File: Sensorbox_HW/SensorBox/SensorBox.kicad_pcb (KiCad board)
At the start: 2 copper layers, 77 parts, among them U1 BME280, U11 PS1-O3-100, U12 DS3231M, U13 OPA197xD, U2 OPA197xD, U4 MC33063AD, U5 OPA197xD, U6 MAX31855EASA, U8 HPP845E131R5

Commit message: Sensorbox
Layout erstellt
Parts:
- moved JP1 228.2 mm to (137.0, 49.5), turned to 180 degrees
- moved U7 225.0 mm to (87.5, 61.2), turned to 180 degrees
- moved C2 218.2 mm to (119.9, 98.4), turned to 90 degrees
- moved C1 217.6 mm to (118.0, 98.3), turned to 90 degrees
- moved D4 215.9 mm to (110.5, 54.0), turned to 90 degrees
- moved U1 214.7 mm to (124.0, 97.5), turned to 180 degrees
- moved ADC1 212.6 mm to (135.5, 36.1), turned to -90 degrees
- moved VCC1 212.3 mm to (135.5, 25.9), turned to -90 degrees
- moved GND1 212.2 mm to (135.5, 33.5), turned to -90 degrees
- moved SDA/Signal1 212.0 mm to (135.5, 28.5), turned to -90 degrees
- moved SCL1 212.0 mm to (135.5, 31.0), turned to -90 degrees
- moved U11 211.9 mm to (128.2, 65.0), turned to -90 degrees
- moved D2 210.3 mm to (103.5, 54.1), turned to 90 degrees
- moved C11 207.9 mm to (125.2, 77.5), turned to -90 degrees
- moved U6 207.9 mm to (125.0, 48.5), turned to 180 degrees
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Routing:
- net VDD_3V3: track 0.00 -> 307.6 mm, vias 0 -> 6
- net VDD_5V: track 0.00 -> 261.3 mm, vias 0 -> 3
- net SDA_GPIO21: track 0.00 -> 232.7 mm, vias 0 -> 5
- net SCL_GPIO22: track 0.00 -> 221.9 mm, vias 0 -> 3
- net Mosi_GPIO23: track 0.00 -> 95.9 mm, vias 0 -> 1
- net Miso_GPIO19: track 0.00 -> 89.5 mm, vias 0 -> 2
- net CS_GPIO15: track 0.00 -> 82.4 mm, vias 0 -> 1
- net SCK_GPIO18: track 0.00 -> 80.4 mm, vias 0 -> 2
- net CS_GPIO5: track 0.00 -> 71.1 mm
- net RTC_INIT_GPIO4: track 0.00 -> 59.2 mm, vias 0 -> 1
- net Miso_GPIO12: track 0.00 -> 53.4 mm, vias 0 -> 1
- net RTC_32Khz_GPIO25: track 0.00 -> 52.9 mm, vias 0 -> 1
- net extern_Sensor_Gpio_33: track 0.00 -> 51.1 mm
- net VCC_Bat: track 0.00 -> 50.9 mm
- net VDD_2.5V: track 0.00 -> 47.2 mm, vias 0 -> 1
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- added copper zone on B.Cu, net GND1
- added copper zone on F.Cu, net GND1
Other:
- board outline added: 128.5 x 97.5 mm

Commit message: Layout fertiggestellt
Layout überarbeitet und fertig gestellt
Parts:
- removed D4: 1.5KExxA, Diode_THT:D_DO-201AE_P15.24mm_Horizontal
- removed R14: 4.7k, Resistor_SMD:R_0402_1005Metric
- added C13: 0.1uF, Capacitor_SMD:C_0402_1005Metric_Pad0.74x0.62mm_HandSolder, F.Cu at (105.7, 64.5)
- added C3: 0.1uF, Capacitor_SMD:C_0402_1005Metric_Pad0.74x0.62mm_HandSolder, F.Cu at (111.4, 64.5)
- added C7: 0.1uF, Capacitor_SMD:C_0402_1005Metric_Pad0.74x0.62mm_HandSolder, F.Cu at (120.4, 63.8)
- added D7: PESD3V3U1UA, Diode_SMD:D_SOD-323, F.Cu at (130.0, 27.2)
- added R3: 100R, Resistor_SMD:R_0402_1005Metric, F.Cu at (130.6, 25.1)
- added R4: 100R, Resistor_SMD:R_0402_1005Metric, F.Cu at (131.8, 33.0)
- added R5: 4.7k, Resistor_SMD:R_0402_1005Metric, F.Cu at (78.0, 68.6)
- CO1: value 45.54µF -> 47µF
- D2: value 1.5KExxA -> PESD3V3U1UA; footprint Diode_THT:D_DO-201AE_P15.24mm_Horizontal -> Diode_SMD:D_SOD-323
- L1: value 52µH -> 51µH; footprint Inductor_SMD:L_0402_1005Metric_Pad0.77x0.64mm_HandSolder -> Inductor_SMD:L_0805_2012Metric_Pad1.05x1.20mm_HandSolder
- Rsc1: value 0R41 -> 0R39
- moved TP7 0.31 mm to (74.7, 68.1)
- moved C8 0.20 mm to (73.2, 77.0)
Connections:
- D2 pad 1: SCL_GPIO22 -> Net-(D2-K)
- SCL1 pad 1: SCL_GPIO22 -> Net-(D2-K)
- SDA/Signal1 pad 1: SDA_GPIO21 -> Net-(D7-K)
- U13 pad 7: VDD_5V -> Net-(U13-V+)
- U2 pad 7: VDD_3V3 -> Net-(U2-V+)
- U5 pad 7: VDD_5V -> Net-(U5-V+)
- U7 pad 26: unconnected-(U7-GND-Pad26) -> GND1
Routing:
- net Net-(D2-K): track 0.00 -> 56.6 mm, vias 0 -> 2
- net Net-(D7-K): track 0.00 -> 10.3 mm, vias 0 -> 1
- net VDD_3V3: track 307.6 -> 316.3 mm
- net VDD_5V: track 261.3 -> 254.3 mm, vias 3 -> 5
- net SDA_GPIO21: track 232.7 -> 226.5 mm, vias 5 -> 6
- net Net-(U2-V+): track 0.00 -> 3.88 mm
- net RTC_INIT_GPIO4: track 59.2 -> 62.8 mm
- net Net-(U13-V+): track 0.00 -> 3.11 mm
- net Net-(U5-V+): track 0.00 -> 2.77 mm
- net VDD_2.5V: track 47.2 -> 44.7 mm
- net SCL_GPIO22: track 221.9 -> 219.7 mm
- net RTC_RST_GPIO16: track 46.6 -> 44.8 mm
- net Net-(U4-Ipk): track 26.4 -> 26.9 mm
- net GND1: track 5.78 -> 5.74 mm, vias 48 -> 52

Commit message: Layout fertigstellen
Löcher, Text auf platine
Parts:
- moved TP5 6.53 mm to (57.1, 52.1), turned to 90 degrees
- moved BT1 2.99 mm to (24.4, 64.1)
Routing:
- net Mosi_GPIO23: track 95.9 -> 97.3 mm
- net Net-(D3-A1): track 28.4 -> 29.7 mm
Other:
- outline, holes or cut-outs redrawn
- board text added: "SensorBox V3"
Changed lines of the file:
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@@
 	(footprint "TestPoint:TestPoint_Loop_D1.80mm_Drill1.0mm_Beaded"
 		(layer "F.Cu")
-		(at 56 58.5)
+		(at 57.15 52.07 90)
 		(descr "wire loop with bead as test point, loop diameter 1.8mm, hole diameter 1.0mm")
 		(tags "test point wire loop bead")
 		(property "Reference" "TP5"
-			(at 0.7 2.5 0)
+			(at 0.7 2.5 90)
 			(layer "F.SilkS")
 			(effects
@@
 		)
 		(property "Value" "TestPoint"
-			(at 0 -2.8 0)
+			(at 0 -2.8 90)
 			(layer "F.Fab")
 			(effects
@@
 		)
 		(property "Footprint" "TestPoint:TestPoint_Loop_D1.80mm_Drill1.0mm_Beaded"
-			(at 0 0 0)
+			(at 0 0 90)
 			(unlocked yes)
 			(layer "F.Fab")
@@
 		)
 		(property "Datasheet" ""
-			(at 0 0 0)
+			(at 0 0 90)
 			(unlocked yes)
 			(layer "F.Fab")
@@
 		)
 		(property "Description" "test point"
-			(at 0 0 0)
+			(at 0 0 90)
 			(unlocked yes)
 			(layer "F.Fab")
@@
 		)
 		(fp_line
-			(start -0.9 -0.2)
-			(end 0.9 -0.2)
+			(start 0.9 -0.2)
+			(end 0.9 0.2)
 			(stroke
 				(width 0.12)
@@
 		)
 		(fp_line
-			(start -0.9 0.2)
-			(end -0.9 -0.2)
+			(start -0.9 -0.2)
+			(end 0.9 -0.2)
 			(stroke
 				(width 0.12)
@@
 		)
 		(fp_line
-			(start 0.9 -0.2)
-			(end 0.9 0.2)
+			(start 0.9 0.2)
+			(end -0.9 0.2)
 			(stroke
 				(width 0.12)
@@
 		)
 		(fp_line
-			(start 0.9 0.2)
-			(end -0.9 0.2)
+			(start -0.9 0.2)
+			(end -0.9 -0.2)
 			(stroke
 				(width 0.12)
@@
 		)
 		(fp_text user "${REFERENCE}"
-			(at 0.7 2.5 0)
+			(at 0.7 2.5 90)
 			(layer "F.Fab")
 			(effects
@@
 		)
 		(pad "1" thru_hole circle
-			(at 0 0)
+			(at 0 0 90)
 			(size 2 2)
 			(drill 1)
@@
 	(footprint "Battery_Basket:BatteryHolder_Keystone_2479_3xAAA"
 		(layer "F.Cu")
-		(at 21.3925 64.0825 90)
+		(at 24.384 64.0825 90)
 		(descr "Keystone Battery Holder, 2479, Battery Type 3xAAA (Script generated with StandardBox.py) (Keystone Battery Holder, 2479, Battery Type 3xAAA)")
 		(tags "Keystone Battery Holder 2479 Battery Type 3xAAA")
@@
 		)
 	)
+	(gr_circle
+		(center 13.716 108.204)
+		(end 13.716 107.188)
+		(stroke
+			(width 0.05)
+			(type default)
+		)
+		(fill none)
+		(layer "Edge.Cuts")
+	)
 	(gr_rect
 		(start 12 12.5)
@@
 		(layer "Edge.Cuts")
 	)
+	(gr_circle
+		(center 138.684 108.204)
+		(end 138.684 107.188)
+		(stroke
+			(width 0.05)
+			(type default)
+		)
+		(fill none)
+		(layer "Edge.Cuts")
+	)
+	(gr_circle
+		(center 13.716 14.224)
+		(end 13.716 13.208)
+		(stroke
+			(width 0.05)
+			(type default)
+		)
+		(fill none)
+		(layer "Edge.Cuts")
+	)
+	(gr_circle
+		(center 138.684 14.224)
+		(end 138.684 13.208)
+		(stroke
+			(width 0.05)
+			(type default)
+		)
+		(fill none)
+		(layer "Edge.Cuts")
+	)
+	(gr_text "SensorBox V3"
+		(at 136.906 107.95 90)
+		(layer "F.SilkS")
+		(effects
+			(font
+				(size 3 3)
+				(thickness 0.3)
+				(bold yes)
+			)
+			(justify left bottom)
+		)
+	)
 	(segment
 		(start 127.203 43.4)
@@
 	)
 	(segment
+		(start 21.3925 80.518)
+		(end 21.3925 80.9108)
+		(width 0.2)
+		(layer "B.Cu")
+		(net 2)
+	)
+	(segment
+		(start 21.3925 80.518)
+		(end 21.3925 68.5235)
+		(width 0.2)
+		(layer "B.Cu")
+		(net 2)
+	)
+	(segment
+		(start 23.368 66.548)
+		(end 23.368 65.0985)
+		(width 0.2)
+		(layer "B.Cu")
+		(net 2)
+	)
+	(segment
 		(start 16.5 80.46)
 		(end 21.3925 80.46)
@@
 	(segment
 		(start 21.3925 80.46)
-		(end 21.3925 80.9108)
+		(end 21.3925 80.518)
 		(width 0.2)
 		(layer "B.Cu")
@@
 	)
 	(segment
-		(start 25 84.5183)
-		(end 25 86.12)
+		(start 23.368 65.0985)
+		(end 24.384 64.0825)
 		(width 0.2)
 		(layer "B.Cu")
@@
 	)
 	(segment
-		(start 21.3925 64.0825)
-		(end 21.3925 80.46)
+		(start 21.3925 68.5235)
+		(end 23.368 66.548)
+		(width 0.2)
+		(layer "B.Cu")
+		(net 2)
+	)
+	(segment
+		(start 25 84.5183)
+		(end 25 86.12)
 		(width 0.2)
 		(layer "B.Cu")
@@
 	)
 	(via
-		(at 15.5 106)
+		(at 18.034 100.838)
 		(size 0.6)
 		(drill 0.3)
@@
 	)
 	(via
-		(at 137.5 15)
+		(at 129.794 13.716)
 		(size 0.6)
 		(drill 0.3)
@@
 	)
 	(segment
+		(start 58.928 52.07)
+		(end 57.15 52.07)
+		(width 0.2)
+		(layer "F.Cu")
+		(net 17)
+	)
+	(segment
 		(start 111.702 18.2392)
 		(end 112.345 18.2392)
@@
 	)
 	(segment
-		(start 60.843 58.5)
-		(end 60.843 55.6857)
+		(start 60.843 55.6857)
+		(end 59.944 54.7867)
 		(width 0.2)
 		(layer "F.Cu")
@@
 	)
 	(segment
-		(start 56 58.5)
-		(end 60.843 58.5)
+		(start 60.843 58.5)
+		(end 60.843 55.6857)
 		(width 0.2)
 		(layer "F.Cu")
@@
 	)
 	(segment
+		(start 59.944 54.7867)
+		(end 59.944 53.086)
+		(width 0.2)
+		(layer "F.Cu")
+		(net 17)
+	)
+	(segment
 		(start 102.761 18.2392)
 		(end 103.105 18.2392)
@@
 	)
 	(segment
+		(start 59.944 53.086)
+		(end 58.928 52.07)
+		(width 0.2)
+		(layer "F.Cu")
+		(net 17)
+	)
+	(segment
 		(start 102 19)
 		(end 102.761 18.2392)
@@
 			(thermal_gap 0.5)
 			(thermal_bridge_width 0.5)
+			(island_removal_mode 1)
+			(island_area_min 10)
 		)
 		(polygon

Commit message: PCB überarbeitung
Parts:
- removed C6: 100µF, Capacitor_SMD:C_0402_1005Metric_Pad0.74x0.62mm_HandSolder
- removed D6: 1.5KExxA, Diode_THT:D_DO-201AE_P15.24mm_Horizontal
- removed R12, R13: 4.7k, Resistor_SMD:R_0402_1005Metric
- removed TP8, TP9: TestPoint, TestPoint:TestPoint_Loop_D1.80mm_Drill1.0mm_Beaded
- added C14: 100uF - 16V, Capacitor_SMD:CP_Elec_6.3x7.7, F.Cu at (24.5, 95.2)
- added CO2: 33uF - 16V, Capacitor_SMD:C_1812_4532Metric_Pad1.57x3.40mm_HandSolder, F.Cu at (35.3, 95.1)
- added D4: PESD3V3U1UA, Diode_SMD:D_SOD-323, F.Cu at (66.1, 92.8)
- added R2: 10kR, Resistor_SMD:R_1206_3216Metric_Pad1.30x1.75mm_HandSolder, F.Cu at (124.7, 93.2)
- added R6: 20kR, Resistor_SMD:R_1206_3216Metric_Pad1.30x1.75mm_HandSolder, F.Cu at (131.0, 93.2)
- C1, C13, C2, C3, C7: value 0.1uF -> 100nF-50V; footprint Capacitor_SMD:C_0402_1005Metric_Pad0.74x0.62mm_HandSolder -> Capacitor_SMD:C_1206_3216Metric_Pad1.33x1.80mm_HandSolder
- C10, C11, C12, C4, C8, C9, CO4: value 100nF -> 100nF-50V; footprint Capacitor_SMD:C_0402_1005Metric_Pad0.74x0.62mm_HandSolder -> Capacitor_SMD:C_1206_3216Metric_Pad1.33x1.80mm_HandSolder
- C5: value 0.1µF -> 100nF-50V; footprint Capacitor_SMD:C_0402_1005Metric_Pad0.74x0.62mm_HandSolder -> Capacitor_SMD:C_1206_3216Metric_Pad1.33x1.80mm_HandSolder
- CO1: value 47µF -> 33uF - 16V; footprint Capacitor_SMD:C_0402_1005Metric_Pad0.74x0.62mm_HandSolder -> Capacitor_SMD:C_1812_4532Metric_Pad1.57x3.40mm_HandSolder
- CT1: footprint Capacitor_SMD:C_0402_1005Metric_Pad0.74x0.62mm_HandSolder -> Capacitor_SMD:C_1206_3216Metric_Pad1.33x1.80mm_HandSolder
- D1: footprint Diode_THT:D_DO-41_SOD81_P10.16mm_Horizontal -> Diode_SMD:D_SMB-SMC_Universal_Handsoldering
- D3: value 1.5KExxA -> SMBJ5.0A; footprint Diode_THT:D_DO-201AE_P15.24mm_Horizontal -> Diode_SMD:D_SMB_Handsoldering
- D5: value 1.5KExxA -> PESD3V3U1UA; footprint Diode_THT:D_DO-201AE_P15.24mm_Horizontal -> Diode_SMD:D_SOD-323
- L1: value 51µH -> 56µH - 2.1A
- R1, R10, R15, R18, R19, R1_1, R1_3, R1_4, R1_5, R1_6, R20, R21, R3, R33, R4, R5, R7, R8, R9, Rsc1, Rset1, Rx1: footprint Resistor_SMD:R_0402_1005Metric -> Resistor_SMD:R_1206_3216Metric_Pad1.30x1.75mm_HandSolder
- R1_2: footprint Resistor_THT:R_Axial_DIN0204_L3.6mm_D1.6mm_P7.62mm_Horizontal -> Resistor_SMD:R_1206_3216Metric_Pad1.30x1.75mm_HandSolder
- R1_7: value 6k8 -> 2k2; footprint Resistor_SMD:R_0402_1005Metric -> Resistor_SMD:R_1206_3216Metric_Pad1.30x1.75mm_HandSolder
- R2_1: value 2k2 -> 6k8; footprint Resistor_SMD:R_0402_1005Metric -> Resistor_SMD:R_1206_3216Metric_Pad1.30x1.75mm_HandSolder
- moved MicroSD2 97.7 mm to (57.8, 102.8), turned to 180 degrees
- moved R33 92.1 mm to (49.4, 92.3), turned to -90 degrees
- moved C10 92.0 mm to (46.3, 100.9), turned to 90 degrees
- moved R20 88.2 mm to (53.4, 92.3), turned to -90 degrees
- moved U8 85.9 mm to (136.6, 29.2), turned to 0 degrees
- moved R21 83.6 mm to (57.2, 92.3), turned to -90 degrees
- moved C5 80.5 mm to (84.8, 99.3), turned to 180 degrees
- moved C4 78.7 mm to (137.1, 33.3), turned to 180 degrees
- moved JP1 78.3 mm to (83.4, 106.6), turned to 90 degrees
- moved U12 76.1 mm to (106.7, 20.3), turned to 90 degrees
- moved TH2 73.1 mm to (82.0, 102.9), turned to 0 degrees
- moved CR1220 71.1 mm to (105.7, 45.0), turned to 180 degrees
- moved R7 65.8 mm to (126.0, 38.1), turned to 180 degrees
- moved TP4 65.2 mm to (59.7, 16.0)
- moved U1 61.1 mm to (137.1, 37.9)
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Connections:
- C13 pad 1: Net-(U13-V+) -> VDD_5V
- C13 pad 2: VDD_5V -> GND1
- C3 pad 1: Net-(U2-V+) -> VDD_3V3
- C3 pad 2: VDD_3V3 -> GND1
- C7 pad 1: Net-(U5-V+) -> VDD_5V
- C7 pad 2: VDD_5V -> GND1
- C9 pad 1: VDD_5V -> VDD_3V3
- D5 pad 1: Miso_GPIO19 -> Mosi_GPIO23
- R1_2 pad 1: Ozon_out_ADC_GPIO27 -> Net-(R1_2-Pad1)
- TP1 pad 1: Ozon_out_ADC_GPIO27 -> Net-(R1_2-Pad1)
- U13 pad 7: Net-(U13-V+) -> VDD_5V
- U2 pad 7: Net-(U2-V+) -> VDD_3V3
- U5 pad 7: Net-(U5-V+) -> VDD_5V
- U7 pad 34: RST_GPIO2 -> unconnected-(U7-2-Pad34)
- VCC1 pad 1: VDD_5V -> VDD_3V3
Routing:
- net GND1: track 5.74 -> 567.7 mm, vias 52 -> 17
- net SDA_GPIO21: track 226.5 -> 97.0 mm, vias 6 -> 4
- net SCL_GPIO22: track 219.7 -> 100.6 mm, vias 3 -> 2
- net Ozon_out_ADC_GPIO27: track 46.0 -> 113.5 mm, vias 0 -> 2
- net VDD_3V3: track 316.3 -> 381.9 mm, vias 6 -> 10
- net extern_Sensor_Gpio_33: track 51.1 -> 101.8 mm, vias 0 -> 6
- net CS_GPIO15: track 82.4 -> 33.6 mm
- net Net-(D2-K): track 56.6 -> 14.9 mm, vias 2 -> 0
- net Mosi_GPIO23: track 97.3 -> 134.9 mm, vias 1 -> 5
- net VDD_5V: track 254.3 -> 217.6 mm, vias 5 -> 4
- net Net-(C11-Pad1): track 20.7 -> 50.6 mm, vias 1 -> 2
- net SCK_GPIO18: track 80.4 -> 108.1 mm, vias 2 -> 3
- net CS_GPIO5: track 71.1 -> 95.9 mm, vias 0 -> 3
- net Net-(CR1220-+): track 30.7 -> 54.7 mm, vias 0 -> 2
- net RTC_INIT_GPIO4: track 62.8 -> 42.8 mm
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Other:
- outline, holes or cut-outs redrawn

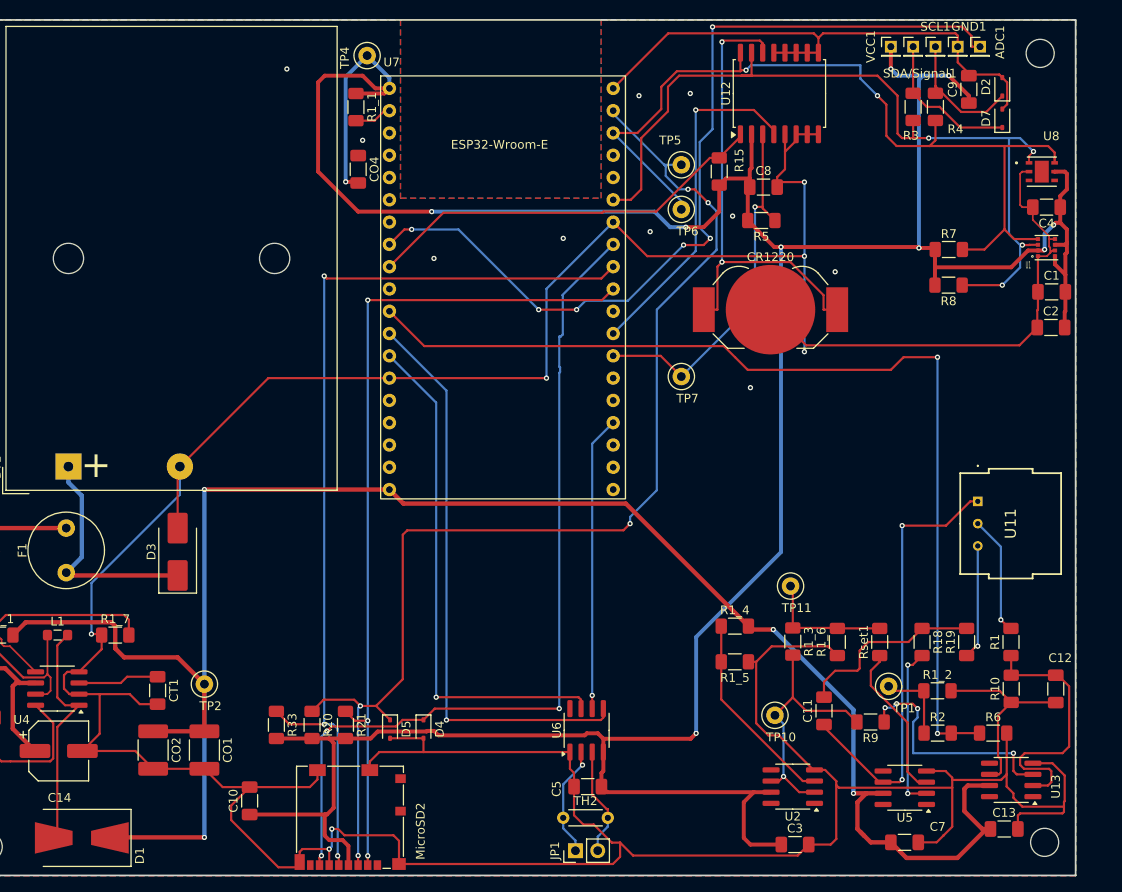
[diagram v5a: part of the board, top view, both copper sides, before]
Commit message: Layout verschönern
Leiterbahnen biem BME verschönert
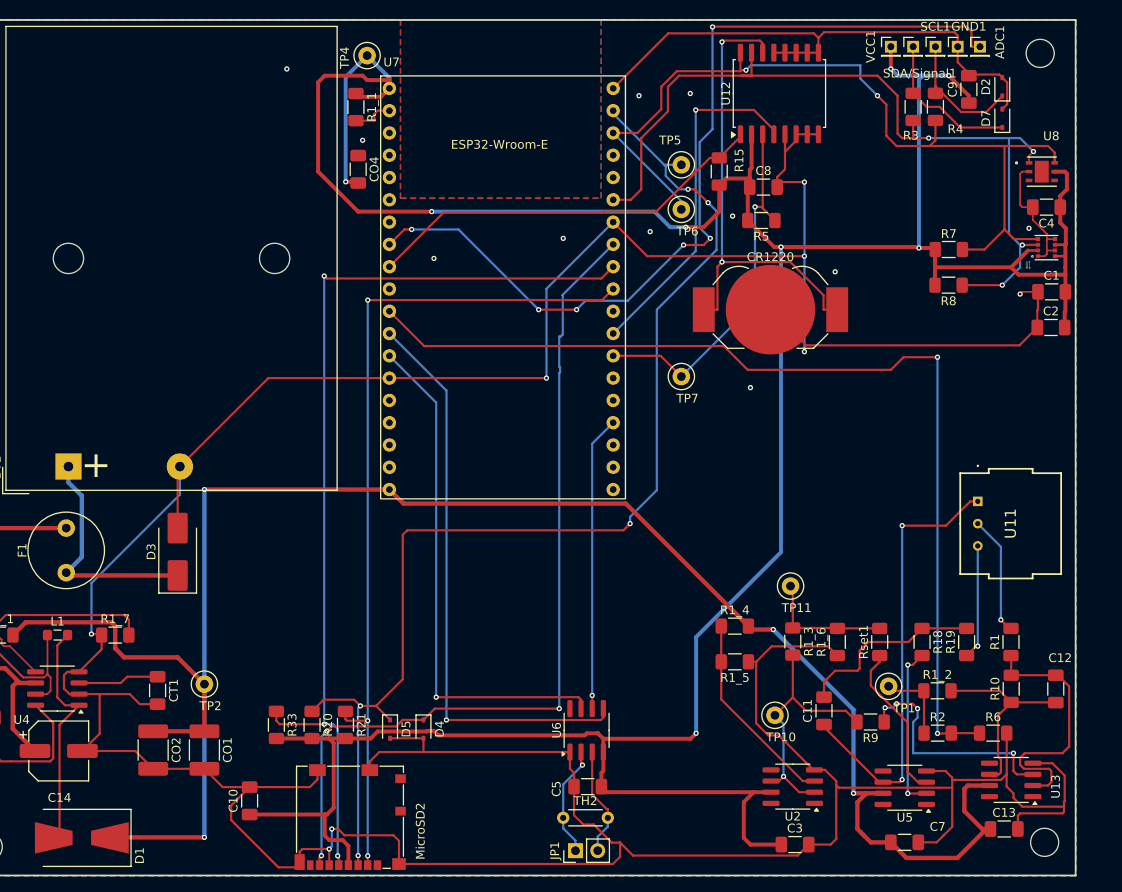
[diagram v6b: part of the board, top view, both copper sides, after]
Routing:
- net GND1: track 567.7 -> 565.9 mm, vias 17 -> 19
- net VDD_3V3: track 381.9 -> 382.6 mm, vias 10 -> 8
- net SCK_GPIO18: track 108.1 -> 108.7 mm
- net CS_GPIO5: track 95.9 -> 96.4 mm
